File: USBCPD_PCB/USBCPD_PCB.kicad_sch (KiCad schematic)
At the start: 64 parts, among them IC1 TMCS1108A3BQDRQ1, IC2 UCC27282QDRQ1, IC3 UCC27282QDRQ1, IC4 BAJ2CC0FP-E2, J1 TB002-500-02BE, J2 TB002-500-02BE, Q1 SIR584DP-T1-RE3, Q2 SIR584DP-T1-RE3, Q3 SIR584DP-T1-RE3, Q4 SIR584DP-T1-RE3, U1 NUCLEO-G474RE

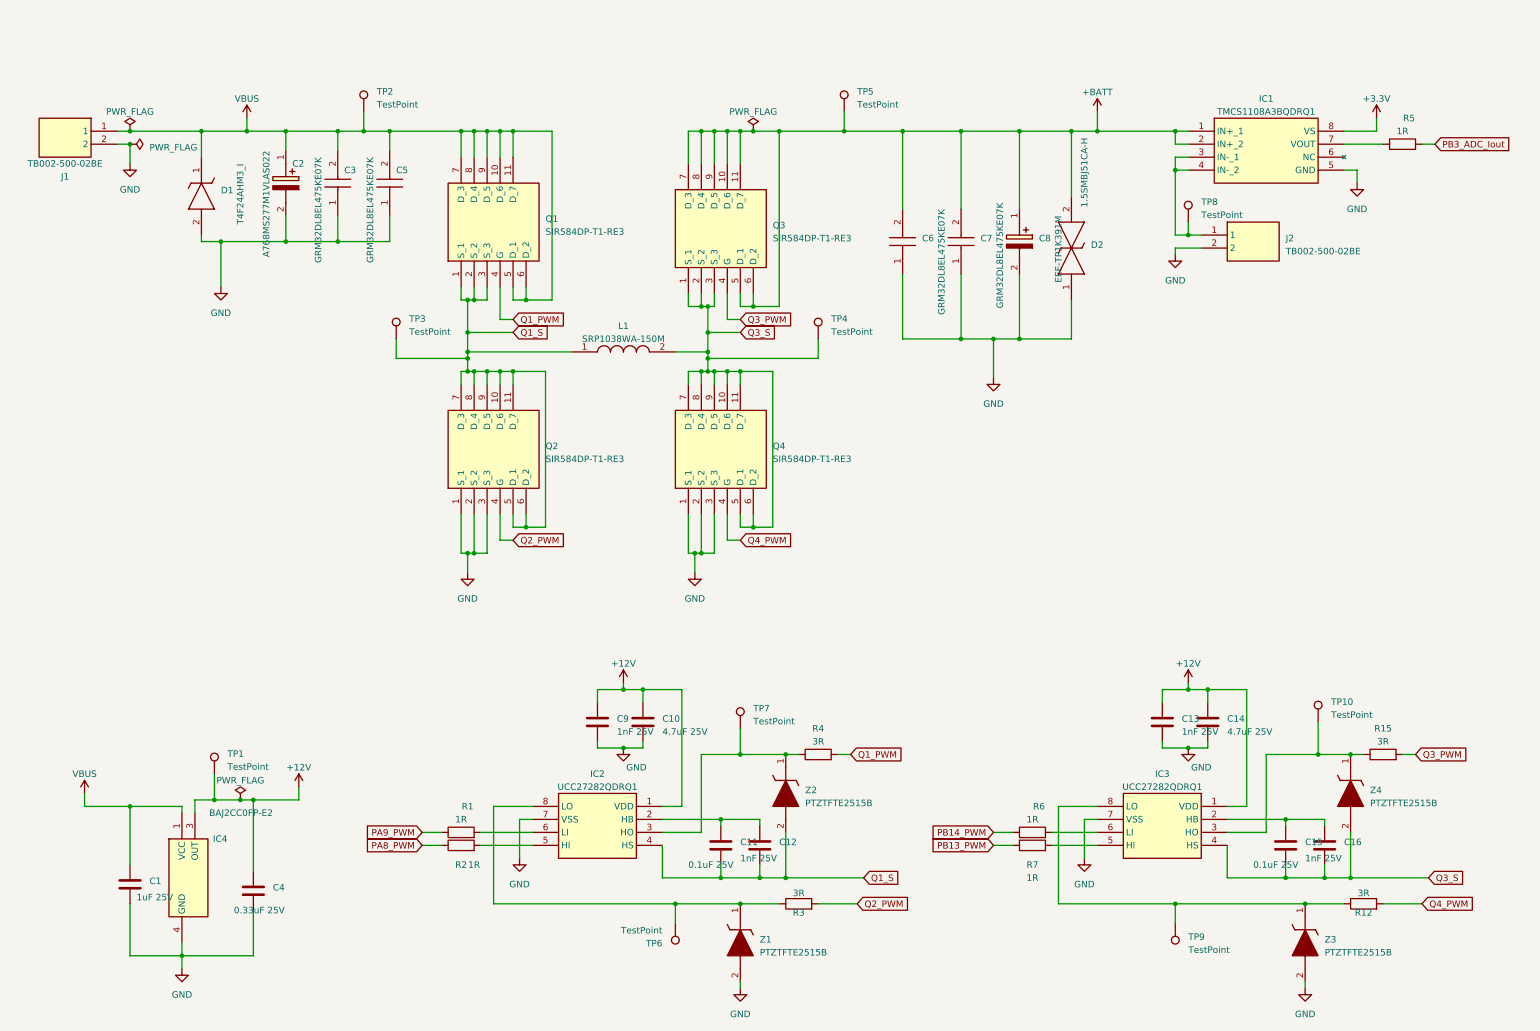
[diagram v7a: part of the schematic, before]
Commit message: Schematic Fixes, Routing started
Removed big zener diodes, replaced with smaller ones
started routing
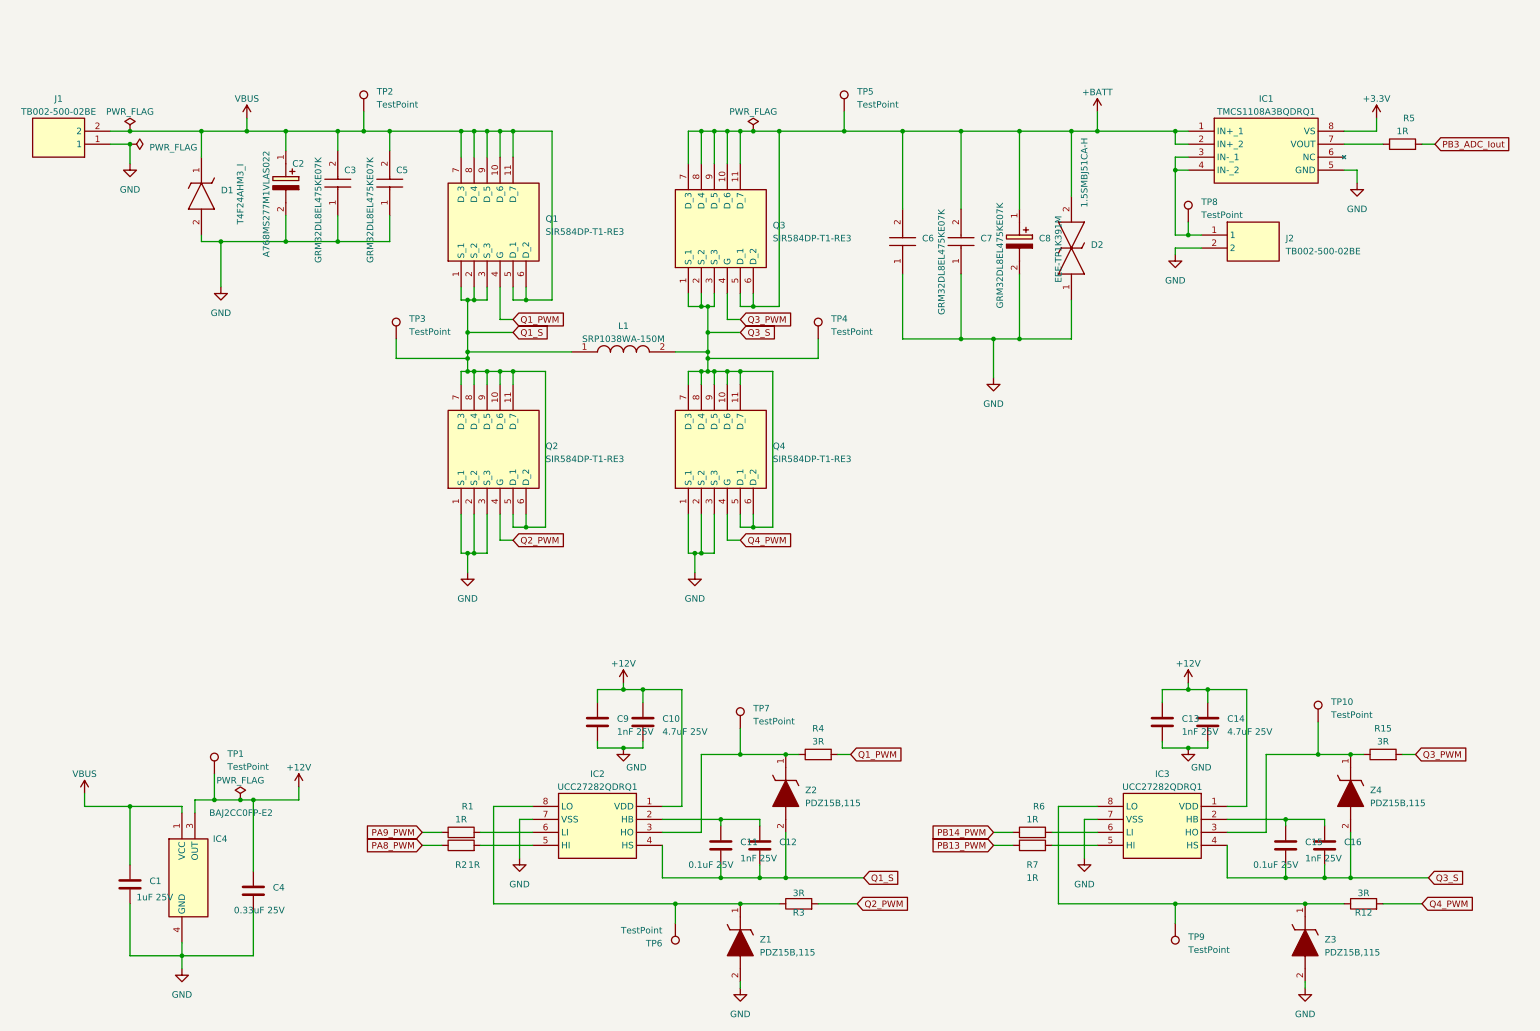
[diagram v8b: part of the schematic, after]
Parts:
- removed Z1, Z2, Z3, Z4: PTZTFTE2515B, PTZTFTE2515B, symbol SamacSys_Parts:PTZTFTE2515B
- added Z1, Z2, Z3, Z4: PDZ15B,115, SOD2512X110N, symbol SamacSys_Parts:PDZ15B,115
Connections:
- net GND: now also J1.1, Z1.2 (A), Z3.2 (A); no longer J1.2
- net Q1_S: now also Z2.2 (A)
- net Q3_S: now also Z4.2 (A)
- net VBUS: now also J1.2; no longer J1.1
- net at IC2.3 (HO), R4.1, TP7.1: now also Z2.1 (K)
- net at IC3.8 (LO), R12.1, TP9.1: now also Z3.1 (K)
- net at IC3.3 (HO), R15.1, TP10.1: now also Z4.1 (K)
- net at IC2.8 (LO), R3.1, TP6.1: now also Z1.1 (K)
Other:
- moved on the sheet: J1
